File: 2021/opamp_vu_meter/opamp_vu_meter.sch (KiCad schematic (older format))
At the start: 43 parts, among them J1 Conn_01x02, J2 Conn_01x02, Q1 Q_PNP_BCE, U1 TLC272, U2 TLC272, U3 TLC272, U4 TLC272, U5 TLC272

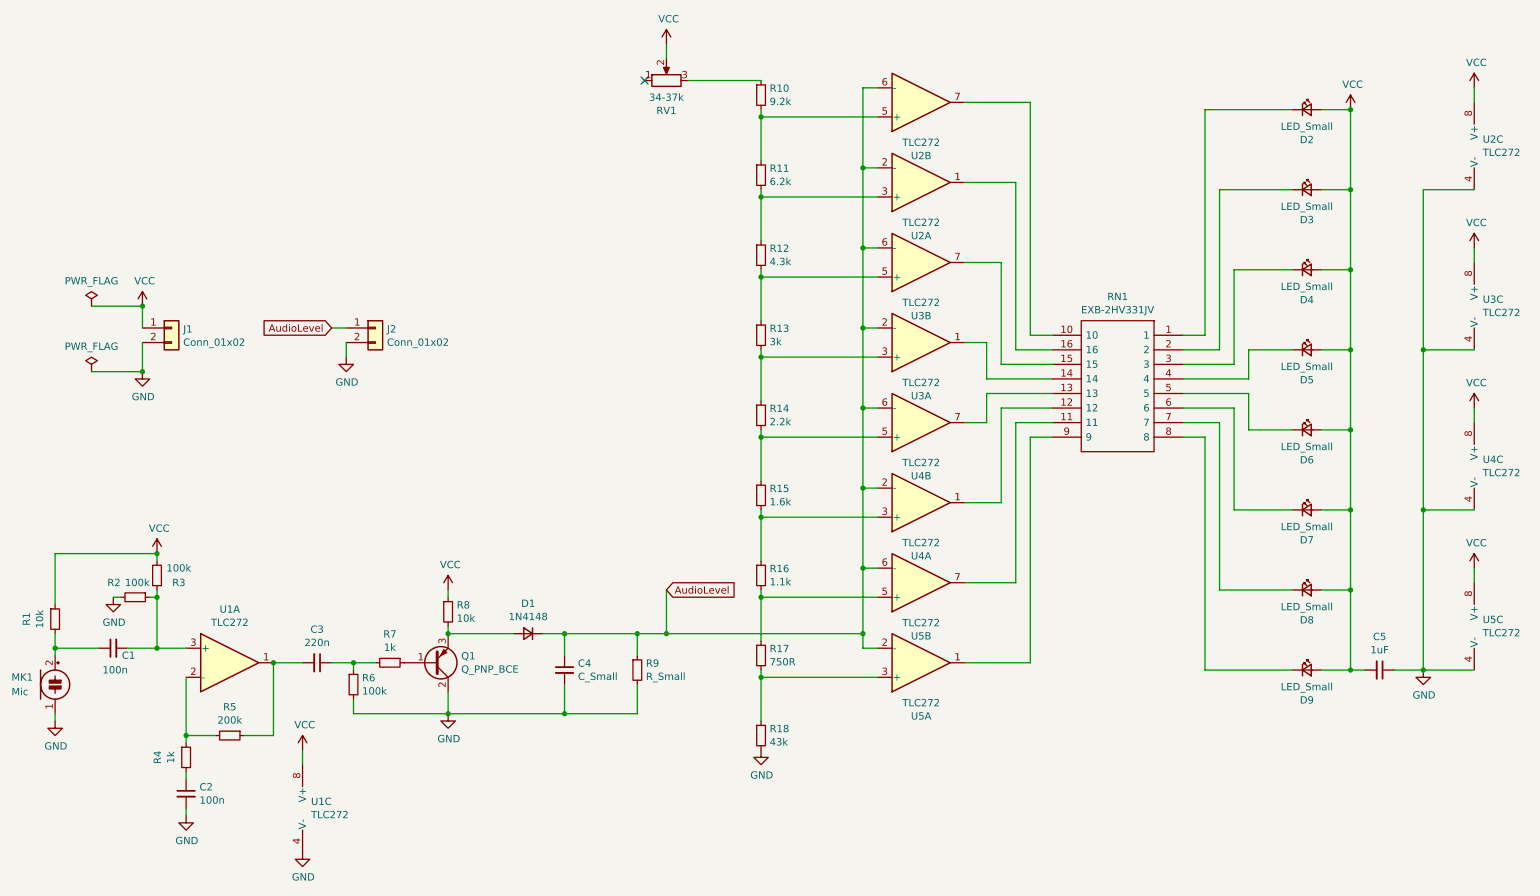
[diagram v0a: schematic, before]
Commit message: Changed outline shape and component placement
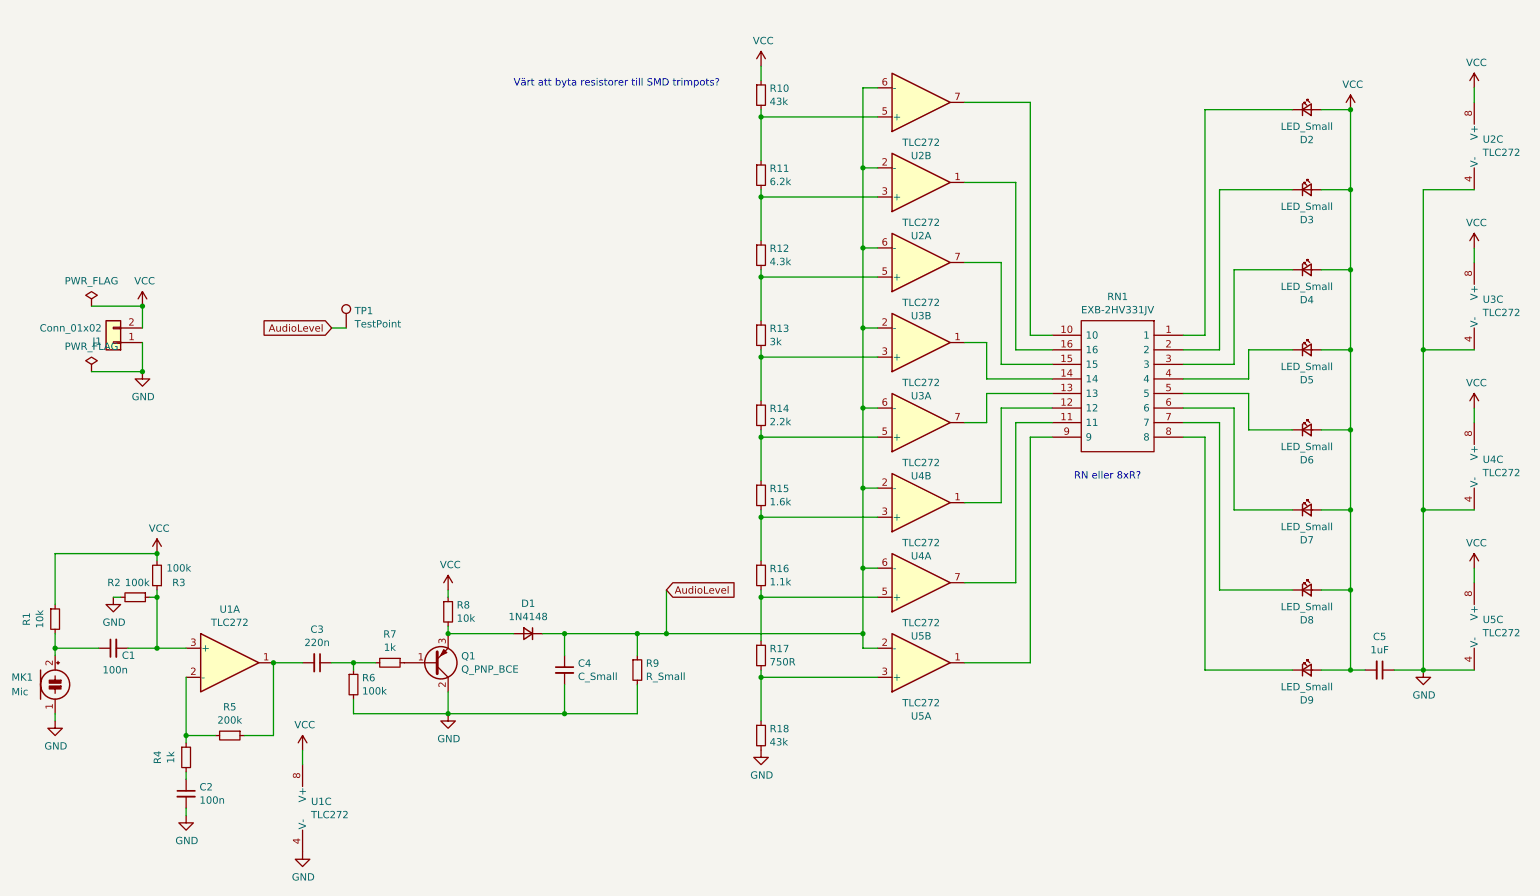
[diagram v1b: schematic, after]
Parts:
- removed J2: Conn_01x02, Connector_PinHeader_2.54mm:PinHeader_1x02_P2.54mm_Vertical, symbol Connector_Generic:Conn_01x02
- removed RV1: 34-37k, Potentiometer_THT:Potentiometer_Bourns_3296W_Vertical, symbol Device:R_POT
- added TP1: TestPoint, TestPoint:TestPoint_Pad_D1.5mm, symbol Connector:TestPoint
- R10: value 9.2k -> 43k
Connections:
- net AudioLevel: now also TP1.1
- net GND: now also J1.1 (Pin_1); no longer J1.2 (Pin_2)
- net VCC: now also J1.2 (Pin_2), R10.1; no longer J1.1 (Pin_1)
- no-connect marks 1 -> 0
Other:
- note added: "RN eller 8xR?"
- note added: "Värt att byta resistorer till SMD trimpots?"
- moved on the sheet: J1
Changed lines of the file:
@@
-$EndComp
-Wire Wire Line
-	2850 3300 2750 3300
-Wire Wire Line
-	2850 3400 2850 3500
-$Comp
-L power:GND #PWR0121
-U 1 1 6170D409
-P 2850 3500
-F 0 "#PWR0121" H 2850 3250 50  0001 C CNN
-F 1 "GND" H 2855 3327 50  0000 C CNN
-F 2 "" H 2850 3500 50  0001 C CNN
-F 3 "" H 2850 3500 50  0001 C CNN
-	1    2850 3500
-	1    0    0    -1
-$EndComp
-Text GLabel 2750 3300 0    50   Input ~ 0
-AudioLevel
-$Comp
-L Connector_Generic:Conn_01x02 J2
-U 1 1 617060B9
-P 3050 3300
-F 0 "J2" H 3130 3292 50  0000 L CNN
-F 1 "Conn_01x02" H 3130 3201 50  0000 L CNN
-F 2 "Connector_PinHeader_2.54mm:PinHeader_1x02_P2.54mm_Vertical" H 3050 3300 50  0001 C CNN
-F 3 "~" H 3050 3300 50  0001 C CNN
-	1    3050 3300
-	1    0    0    -1
 $EndComp
 Wire Wire Line
@@
 L Connector_Generic:Conn_01x02 J1
 U 1 1 618402C3
-P 1650 3300
-F 0 "J1" H 1730 3292 50  0000 L CNN
-F 1 "Conn_01x02" H 1730 3201 50  0000 L CNN
-F 2 "TerminalBlock_Phoenix:TerminalBlock_Phoenix_MKDS-1,5-2-5.08_1x02_P5.08mm_Horizontal" H 1650 3300 50  0001 C CNN
-F 3 "~" H 1650 3300 50  0001 C CNN
-	1    1650 3300
-	1    0    0    -1
+P 1250 3400
+F 0 "J1" H 1330 3392 50  0000 L CNN
+F 1 "Conn_01x02" H 1330 3301 50  0000 L CNN
+F 2 "TerminalBlock_Phoenix:TerminalBlock_Phoenix_MKDS-1,5-2-5.08_1x02_P5.08mm_Horizontal" H 1250 3400 50  0001 C CNN
+F 3 "~" H 1250 3400 50  0001 C CNN
+	1    1250 3400
+	-1   0    0    1
 $EndComp
 $Comp
@@
 	0    1    1    0
 $EndComp
-NoConn ~ 4900 1600
 $Comp
 L Amplifier_Operational:TLC272 U2
@@
 P 5700 1700
 F 0 "R10" H 5759 1746 50  0000 L CNN
-F 1 "9.2k" H 5759 1655 50  0000 L CNN
+F 1 "43k" H 5759 1655 50  0000 L CNN
 F 2 "Resistor_SMD:R_0805_2012Metric_Pad1.20x1.40mm_HandSolder" H 5700 1700 50  0001 C CNN
 F 3 "~" H 5700 1700 50  0001 C CNN
@@
 Connection ~ 6400 4950
 $Comp
-L Device:R_POT RV1
-U 1 1 61613085
-P 5050 1600
-F 0 "RV1" V 4843 1600 50  0000 C CNN
-F 1 "34-37k" V 4934 1600 50  0000 C CNN
-F 2 "Potentiometer_THT:Potentiometer_Bourns_3296W_Vertical" H 5050 1600 50  0001 C CNN
-F 3 "~" H 5050 1600 50  0001 C CNN
-	1    5050 1600
-	0    -1   -1   0
-$EndComp
-$Comp
 L power:VCC #PWR01
 U 1 1 6161C13B
-P 5050 1350
-F 0 "#PWR01" H 5050 1200 50  0001 C CNN
-F 1 "VCC" H 5065 1523 50  0000 C CNN
-F 2 "" H 5050 1350 50  0001 C CNN
-F 3 "" H 5050 1350 50  0001 C CNN
-	1    5050 1350
-	1    0    0    -1
-$EndComp
-Wire Wire Line
-	5050 1350 5050 1450
-Wire Wire Line
-	5200 1600 5700 1600
+P 5700 1500
+F 0 "#PWR01" H 5700 1350 50  0001 C CNN
+F 1 "VCC" H 5715 1673 50  0000 C CNN
+F 2 "" H 5700 1500 50  0001 C CNN
+F 3 "" H 5700 1500 50  0001 C CNN
+	1    5700 1500
+	1    0    0    -1
+$EndComp
+Wire Wire Line
+	5700 1500 5700 1600
 $Comp
 L Device:R_Small R18
@@
 Wire Wire Line
 	8600 3650 9050 3650
+Text GLabel 2750 3300 0    50   Input ~ 0
+AudioLevel
+Wire Wire Line
+	2850 3300 2750 3300
+$Comp
+L Connector:TestPoint TP1
+U 1 1 61B4A93D
+P 2850 3300
+F 0 "TP1" H 2908 3418 50  0000 L CNN
+F 1 "TestPoint" H 2908 3327 50  0000 L CNN
+F 2 "TestPoint:TestPoint_Pad_D1.5mm" H 3050 3300 50  0001 C CNN
+F 3 "~" H 3050 3300 50  0001 C CNN
+	1    2850 3300
+	1    0    0    -1
+$EndComp
+Text Notes 4000 1650 0    50   ~ 0
+Värt att byta resistorer till SMD trimpots?
+Text Notes 7850 4350 0    50   ~ 0
+RN eller 8xR?
 $EndSCHEMATC

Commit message: Final version (hopefully)
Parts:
- removed R10: 43k, Resistor_SMD:R_0805_2012Metric_Pad1.20x1.40mm_HandSolder, symbol Device:R_Small
- removed RN1: EXB-2HV331JV, SamacSys_Parts:EXB2HV331JV, symbol opamp_vu_meter-rescue:EXB-2HV331JV-SamacSys_Parts
- added RN1, RN2: R_Pack04, Resistor_SMD:R_Array_Convex_4x1206, symbol Device:R_Pack04
- added RV1: R_POT, Potentiometer_SMD:Potentiometer_Bourns_TC33X_Vertical, symbol Device:R_POT
- C4: value C_Small -> 220nF
- R5: value 200k -> 100k
- R9: value R_Small -> 220K
- renumbered TP1 to Audiolevel_TP1
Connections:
- net VCC: now also RV1.2
- net at U2.1: now also RN1.2 (R2.1)
- net at R11.1, U2.5 (+): now also RV1.3
- net at U2.7: now also RN1.1 (R1.1)
- net at U3.1: now also RN1.4 (R4.1)
- net at U3.7: now also RN1.3 (R3.1)
- net at U4.1: now also RN2.2 (R2.1)
- net at U4.7: now also RN2.1 (R1.1)
- net at U5.1: now also RN2.4 (R4.1)
- net at U5.7: now also RN2.3 (R3.1)
- net at D2.1 (K): now also RN1.8 (R1.2)
- net at D3.1 (K): now also RN1.7 (R2.2)
- net at D4.1 (K): now also RN1.6 (R3.2)
- net at D5.1 (K): now also RN1.5 (R4.2)
- net at D6.1 (K): now also RN2.8 (R1.2)
- net at D7.1 (K): now also RN2.7 (R2.2)
- net at D8.1 (K): now also RN2.6 (R3.2)
- net at D9.1 (K): now also RN2.5 (R4.2)
- no-connect marks 0 -> 1
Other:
- note removed: "RN eller 8xR?"
- note removed: "Värt att byta resistorer till SMD trimpots?"
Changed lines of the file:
@@
 Wire Wire Line
 	2900 5950 3550 5950
-$Comp
-L Device:C_Small C4
-U 1 1 61681A90
-P 4350 5650
-F 0 "C4" H 4442 5696 50  0000 L CNN
-F 1 "C_Small" H 4442 5605 50  0000 L CNN
-F 2 "Capacitor_SMD:C_0805_2012Metric_Pad1.18x1.45mm_HandSolder" H 4350 5650 50  0001 C CNN
-F 3 "~" H 4350 5650 50  0001 C CNN
-	1    4350 5650
-	1    0    0    -1
-$EndComp
-$Comp
-L Device:R_Small R9
-U 1 1 6167D4EA
-P 4850 5650
-F 0 "R9" H 4909 5696 50  0000 L CNN
-F 1 "R_Small" H 4909 5605 50  0000 L CNN
-F 2 "Resistor_SMD:R_0805_2012Metric_Pad1.20x1.40mm_HandSolder" H 4850 5650 50  0001 C CNN
-F 3 "~" H 4850 5650 50  0001 C CNN
-	1    4850 5650
-	1    0    0    -1
-$EndComp
 Connection ~ 3550 5400
 Wire Wire Line
@@
 P 2050 6100
 F 0 "R5" V 1854 6100 50  0000 C CNN
-F 1 "200k" V 1945 6100 50  0000 C CNN
+F 1 "100k" V 1945 6100 50  0000 C CNN
 F 2 "Resistor_SMD:R_0805_2012Metric_Pad1.20x1.40mm_HandSolder" H 2050 6100 50  0001 C CNN
 F 3 "~" H 2050 6100 50  0001 C CNN
@@
 $EndComp
 $Comp
-L Device:R_Small R10
-U 1 1 615F7525
-P 5700 1700
-F 0 "R10" H 5759 1746 50  0000 L CNN
-F 1 "43k" H 5759 1655 50  0000 L CNN
-F 2 "Resistor_SMD:R_0805_2012Metric_Pad1.20x1.40mm_HandSolder" H 5700 1700 50  0001 C CNN
-F 3 "~" H 5700 1700 50  0001 C CNN
-	1    5700 1700
-	1    0    0    -1
-$EndComp
-$Comp
 L Device:R_Small R11
 U 1 1 615FD4BF
@@
 Connection ~ 6400 4950
 $Comp
-L power:VCC #PWR01
-U 1 1 6161C13B
-P 5700 1500
-F 0 "#PWR01" H 5700 1350 50  0001 C CNN
-F 1 "VCC" H 5715 1673 50  0000 C CNN
-F 2 "" H 5700 1500 50  0001 C CNN
-F 3 "" H 5700 1500 50  0001 C CNN
-	1    5700 1500
-	1    0    0    -1
-$EndComp
-Wire Wire Line
-	5700 1500 5700 1600
-$Comp
 L Device:R_Small R18
 U 1 1 61625DB4
@@
 	1    0    0    -1
 $EndComp
-$Comp
-L opamp_vu_meter-rescue:EXB-2HV331JV-SamacSys_Parts RN1
-U 1 1 6179BC74
-P 8600 3350
-F 0 "RN1" H 9050 3615 50  0000 C CNN
-F 1 "EXB-2HV331JV" H 9050 3524 50  0000 C CNN
-F 2 "SamacSys_Parts:EXB2HV331JV" H 9350 3450 50  0001 L CNN
-F 3 "https://industrial.panasonic.com/cdbs/www-data/pdf/AOC0000/AOC0000C14.pdf" H 9350 3350 50  0001 L CNN
-F 4 "PANASONIC - EXB2HV331JV - RESISTOR,CVEX ARRAY,0402X8, 330R 5%" H 9350 3250 50  0001 L CNN "Description"
-F 5 "0.55" H 9350 3150 50  0001 L CNN "Height"
-F 6 "667-EXB-2HV331JV" H 9350 3050 50  0001 L CNN "Mouser Part Number"
-F 7 "https://www.mouser.co.uk/ProductDetail/Panasonic/EXB-2HV331JV?qs=oE3VwAv%2FYtnCLUI08Bts8A%3D%3D" H 9350 2950 50  0001 L CNN "Mouser Price/Stock"
-F 8 "Panasonic" H 9350 2850 50  0001 L CNN "Manufacturer_Name"
-F 9 "EXB-2HV331JV" H 9350 2750 50  0001 L CNN "Manufacturer_Part_Number"
-	1    8600 3350
-	-1   0    0    -1
-$EndComp
-Wire Wire Line
-	7700 3350 7550 3350
 Wire Wire Line
 	7550 3350 7550 1750
 Wire Wire Line
-	7700 3450 7450 3450
-Wire Wire Line
 	7450 3450 7450 2300
 Wire Wire Line
 	7450 2300 7100 2300
 Wire Wire Line
-	7700 3550 7350 3550
-Wire Wire Line
 	7350 3550 7350 2850
 Wire Wire Line
 	7350 2850 7100 2850
 Wire Wire Line
-	7700 3650 7250 3650
-Wire Wire Line
 	7250 3650 7250 3400
 Wire Wire Line
 	7250 3400 7100 3400
 Wire Wire Line
-	7700 3750 7250 3750
-Wire Wire Line
 	7250 3750 7250 3950
 Wire Wire Line
 	7250 3950 7100 3950
 Wire Wire Line
-	7700 3850 7350 3850
-Wire Wire Line
 	7350 3850 7350 4500
 Wire Wire Line
 	7350 4500 7100 4500
 Wire Wire Line
-	7700 3950 7450 3950
-Wire Wire Line
 	7450 3950 7450 5050
 Wire Wire Line
 	7450 5050 7100 5050
-Wire Wire Line
-	7700 4050 7550 4050
 Wire Wire Line
 	7550 4050 7550 5600
@@
 	9050 3650 9050 3450
 Wire Wire Line
-	8600 3550 8950 3550
-Wire Wire Line
 	8950 3550 8950 2900
 Wire Wire Line
-	8600 3450 8850 3450
-Wire Wire Line
 	8850 3450 8850 2350
-Wire Wire Line
-	8600 3350 8750 3350
 Wire Wire Line
 	8750 3350 8750 1800
@@
 Wire Wire Line
 	10050 5650 10250 5650
-Wire Wire Line
-	8600 4050 8750 4050
-Wire Wire Line
-	8600 3950 8850 3950
-Wire Wire Line
-	8600 3850 8950 3850
-Wire Wire Line
-	8600 3750 9050 3750
-Wire Wire Line
-	8600 3650 9050 3650
 Text GLabel 2750 3300 0    50   Input ~ 0
 AudioLevel
@@
 	2850 3300 2750 3300
 $Comp
-L Connector:TestPoint TP1
+L Connector:TestPoint Audiolevel_TP1
 U 1 1 61B4A93D
 P 2850 3300
-F 0 "TP1" H 2908 3418 50  0000 L CNN
+F 0 "Audiolevel_TP1" H 2908 3418 50  0000 L CNN
 F 1 "TestPoint" H 2908 3327 50  0000 L CNN
 F 2 "TestPoint:TestPoint_Pad_D1.5mm" H 3050 3300 50  0001 C CNN
@@
 	1    0    0    -1
 $EndComp
-Text Notes 4000 1650 0    50   ~ 0
-Värt att byta resistorer till SMD trimpots?
-Text Notes 7850 4350 0    50   ~ 0
-RN eller 8xR?
+$Comp
+L Device:R_Small R9
+U 1 1 6167D4EA
+P 4850 5650
+F 0 "R9" H 4909 5696 50  0000 L CNN
+F 1 "220K" H 4909 5605 50  0000 L CNN
+F 2 "Resistor_SMD:R_0805_2012Metric_Pad1.20x1.40mm_HandSolder" H 4850 5650 50  0001 C CNN
+F 3 "~" H 4850 5650 50  0001 C CNN
+	1    4850 5650
+	1    0    0    -1
+$EndComp
+$Comp
+L Device:C_Small C4
+U 1 1 61681A90
+P 4350 5650
+F 0 "C4" H 4442 5696 50  0000 L CNN
+F 1 "220nF" H 4442 5605 50  0000 L CNN
+F 2 "Capacitor_SMD:C_0805_2012Metric_Pad1.18x1.45mm_HandSolder" H 4350 5650 50  0001 C CNN
+F 3 "~" H 4350 5650 50  0001 C CNN
+	1    4350 5650
+	1    0    0    -1
+$EndComp
+Wire Wire Line
+	5600 1800 5700 1800
+$Comp
+L Device:R_POT RV1
+U 1 1 6190E703
+P 5450 1800
+F 0 "RV1" V 5335 1800 50  0000 C CNN
+F 1 "R_POT" V 5244 1800 50  0000 C CNN
+F 2 "Potentiometer_SMD:Potentiometer_Bourns_TC33X_Vertical" H 5450 1800 50  0001 C CNN
+F 3 "~" H 5450 1800 50  0001 C CNN
+	1    5450 1800
+	0    -1   -1   0
+$EndComp
+$Comp
+L power:VCC #PWR01
+U 1 1 6161C13B
+P 5450 1650
+F 0 "#PWR01" H 5450 1500 50  0001 C CNN
+F 1 "VCC" H 5465 1823 50  0000 C CNN
+F 2 "" H 5450 1650 50  0001 C CNN
+F 3 "" H 5450 1650 50  0001 C CNN
+	1    5450 1650
+	1    0    0    -1
+$EndComp
+NoConn ~ 5300 1800
+$Comp
+L Device:R_Pack04 RN1
+U 1 1 6198A202
+P 8100 3550
+F 0 "RN1" V 7683 3550 50  0000 C CNN
+F 1 "R_Pack04" V 7774 3550 50  0000 C CNN
+F 2 "Resistor_SMD:R_Array_Convex_4x1206" V 8375 3550 50  0001 C CNN
+F 3 "~" H 8100 3550 50  0001 C CNN
+	1    8100 3550
+	0    1    1    0
+$EndComp
+$Comp
+L Device:R_Pack04 RN2
+U 1 1 61987DDD
+P 8100 3950
+F 0 "RN2" V 8425 3950 50  0000 C CNN
+F 1 "R_Pack04" V 8334 3950 50  0000 C CNN
+F 2 "Resistor_SMD:R_Array_Convex_4x1206" V 8375 3950 50  0001 C CNN
+F 3 "~" H 8100 3950 50  0001 C CNN
+	1    8100 3950
+	0    1    1    0
+$EndComp
+Wire Wire Line
+	7550 3350 7900 3350
+Wire Wire Line
+	7450 3450 7900 3450
+Wire Wire Line
+	7350 3550 7900 3550
+Wire Wire Line
+	7250 3650 7900 3650
+Wire Wire Line
+	7250 3750 7900 3750
+Wire Wire Line
+	7350 3850 7900 3850
+Wire Wire Line
+	7450 3950 7900 3950
+Wire Wire Line
+	7550 4050 7900 4050
+Wire Wire Line
+	8300 4050 8750 4050
+Wire Wire Line
+	8300 3950 8850 3950
+Wire Wire Line
+	8300 3850 8950 3850
+Wire Wire Line
+	8300 3750 9050 3750
+Wire Wire Line
+	8300 3650 9050 3650
+Wire Wire Line
+	8300 3550 8950 3550
+Wire Wire Line
+	8300 3450 8850 3450
+Wire Wire Line
+	8300 3350 8750 3350
 $EndSCHEMATC

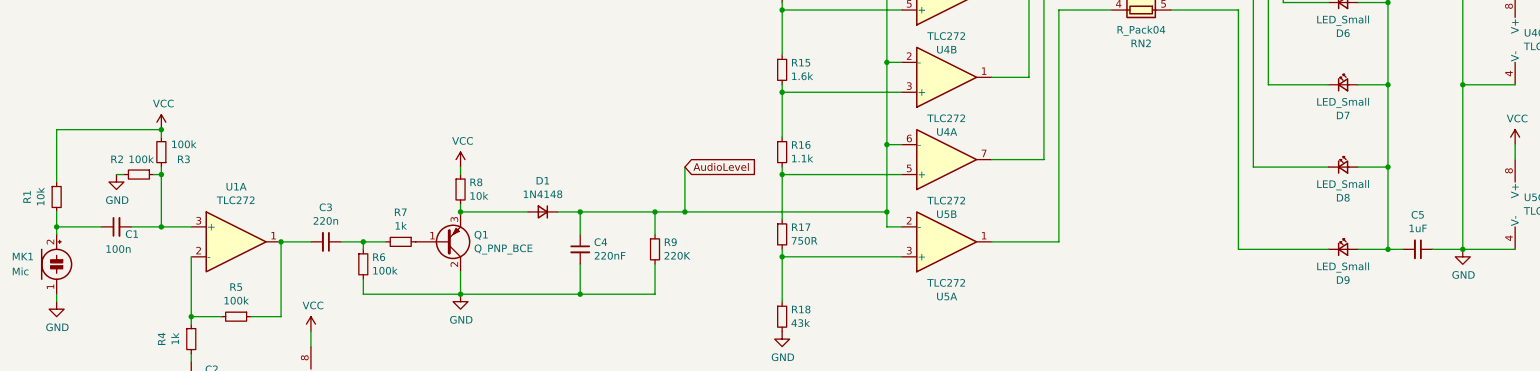
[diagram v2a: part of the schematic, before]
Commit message: Minor revision with zener to stabilize
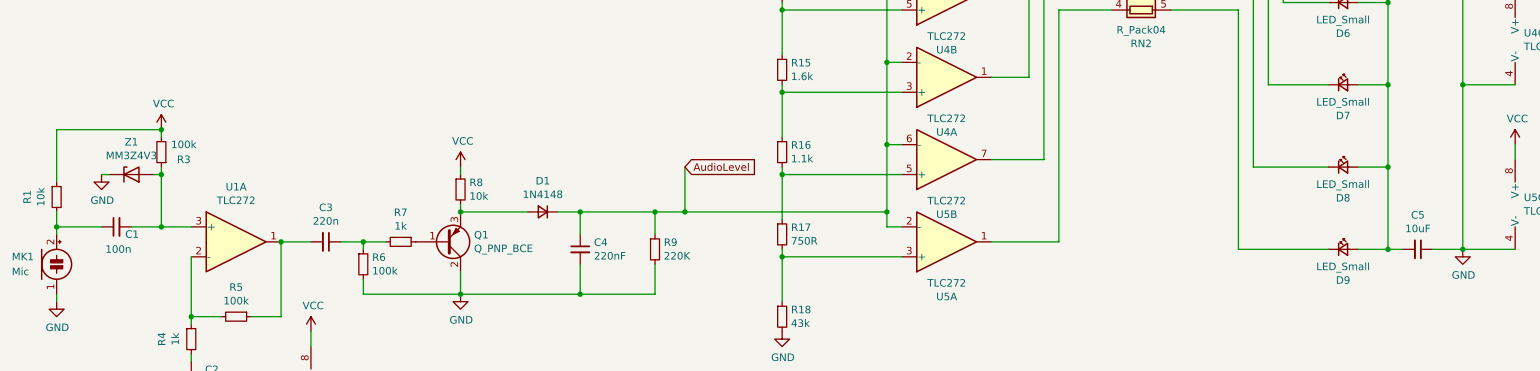
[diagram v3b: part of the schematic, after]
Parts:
- removed R2: 100k, Resistor_SMD:R_0805_2012Metric_Pad1.20x1.40mm_HandSolder, symbol Device:R_Small
- added Z1: MM3Z4V3, Diode_SMD:D_SOD-123F, symbol Diode:MM3Zxx
- C5: value 1uF -> 10uF
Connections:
- net GND: now also Z1.1 (K)
- net at C1.2, R3.1, U1.3 (+): now also Z1.2 (A)
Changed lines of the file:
@@
 	1550 5500 1750 5500
 Wire Wire Line
-	1300 5150 1250 5150
+	1200 5150 1150 5150
 $Comp
 L power:GND #PWR0113
 U 1 1 617A4917
-P 1250 5150
-F 0 "#PWR0113" H 1250 4900 50  0001 C CNN
-F 1 "GND" H 1255 4977 50  0000 C CNN
-F 2 "" H 1250 5150 50  0001 C CNN
-F 3 "" H 1250 5150 50  0001 C CNN
-	1    1250 5150
+P 1150 5150
+F 0 "#PWR0113" H 1150 4900 50  0001 C CNN
+F 1 "GND" H 1155 4977 50  0000 C CNN
+F 2 "" H 1150 5150 50  0001 C CNN
+F 3 "" H 1150 5150 50  0001 C CNN
+	1    1150 5150
 	1    0    0    -1
 $EndComp
@@
 $EndComp
 $Comp
-L Device:R_Small R2
-U 1 1 617160CD
-P 1400 5150
-F 0 "R2" V 1300 5050 50  0000 R CNN
-F 1 "100k" V 1300 5250 50  0000 R CNN
-F 2 "Resistor_SMD:R_0805_2012Metric_Pad1.20x1.40mm_HandSolder" H 1400 5150 50  0001 C CNN
-F 3 "~" H 1400 5150 50  0001 C CNN
-	1    1400 5150
-	0    1    1    0
-$EndComp
-$Comp
 L power:VCC #PWR0112
 U 1 1 6171490D
@@
 P 9950 5650
 F 0 "C5" V 9721 5650 50  0000 C CNN
-F 1 "1uF" V 9812 5650 50  0000 C CNN
+F 1 "10uF" V 9812 5650 50  0000 C CNN
 F 2 "Capacitor_SMD:C_0805_2012Metric_Pad1.18x1.45mm_HandSolder" H 9950 5650 50  0001 C CNN
 F 3 "~" H 9950 5650 50  0001 C CNN
@@
 Wire Wire Line
 	8300 3350 8750 3350
+$Comp
+L Diode:MM3Zxx Z1
+U 1 1 61B2A748
+P 1350 5150
+F 0 "Z1" H 1350 5367 50  0000 C CNN
+F 1 "MM3Z4V3" H 1350 5276 50  0000 C CNN
+F 2 "Diode_SMD:D_SOD-123F" H 1350 4975 50  0001 C CNN
+F 3 "https://diotec.com/tl_files/diotec/files/pdf/datasheets/mm3z2v4.pdf" H 1350 5150 50  0001 C CNN
+	1    1350 5150
+	1    0    0    -1
+$EndComp
 $EndSCHEMATC
